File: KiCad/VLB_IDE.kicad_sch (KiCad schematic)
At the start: 9 parts, among them J16 Secondary IDE, U15 OPTI_82C611A

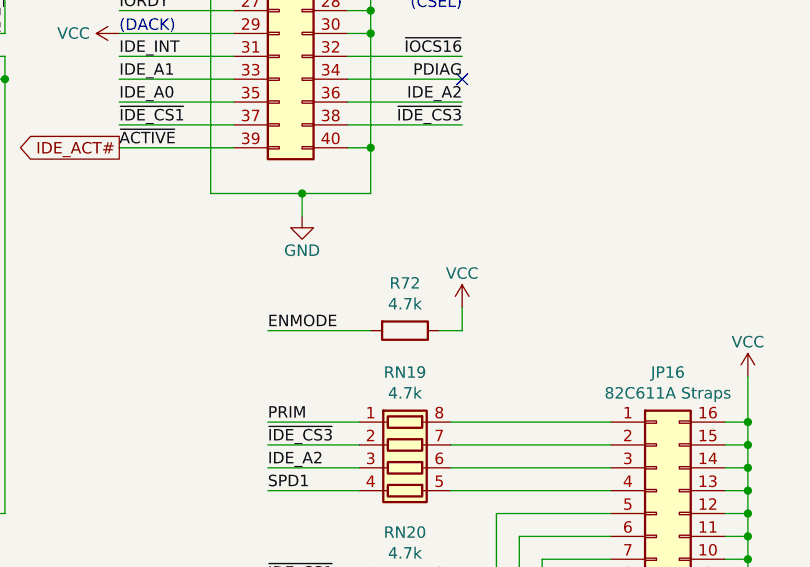
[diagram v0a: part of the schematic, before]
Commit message: Version 0.3: Update DRAM schematic, pull-ups/pull-downs, CPU configuration jumpers
Signed-off-by: Sergey Kiselev <skiselev@gmail.com>
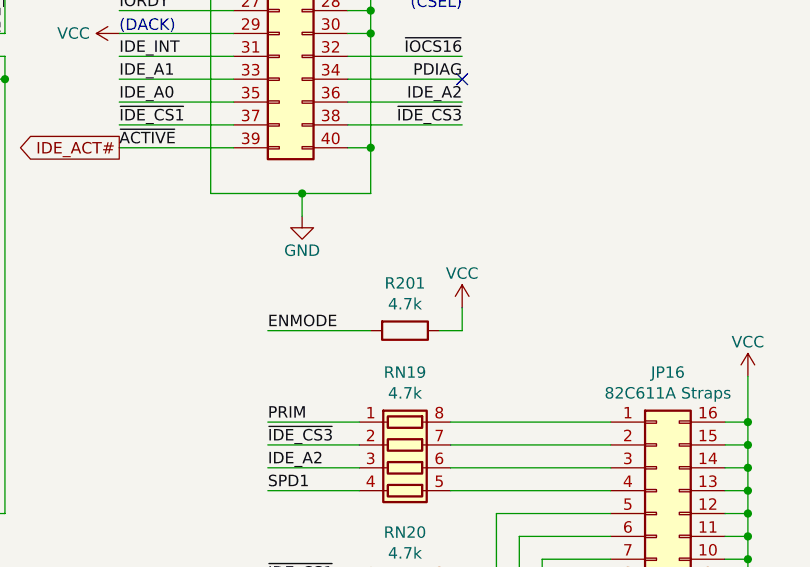
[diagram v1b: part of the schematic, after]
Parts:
- renumbered R72 to R201
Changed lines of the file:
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@@
   (symbol (lib_id "Device:R") (at 196.85 101.6 270) (unit 1)
     (in_bom yes) (on_board yes)
-    (property "Reference" "R72" (id 0) (at 196.85 96.3422 90))
+    (property "Reference" "R201" (id 0) (at 196.85 96.3422 90))
     (property "Value" "4.7k" (id 1) (at 196.85 98.6536 90))
     (property "Footprint" "" (id 2) (at 196.85 99.822 90)

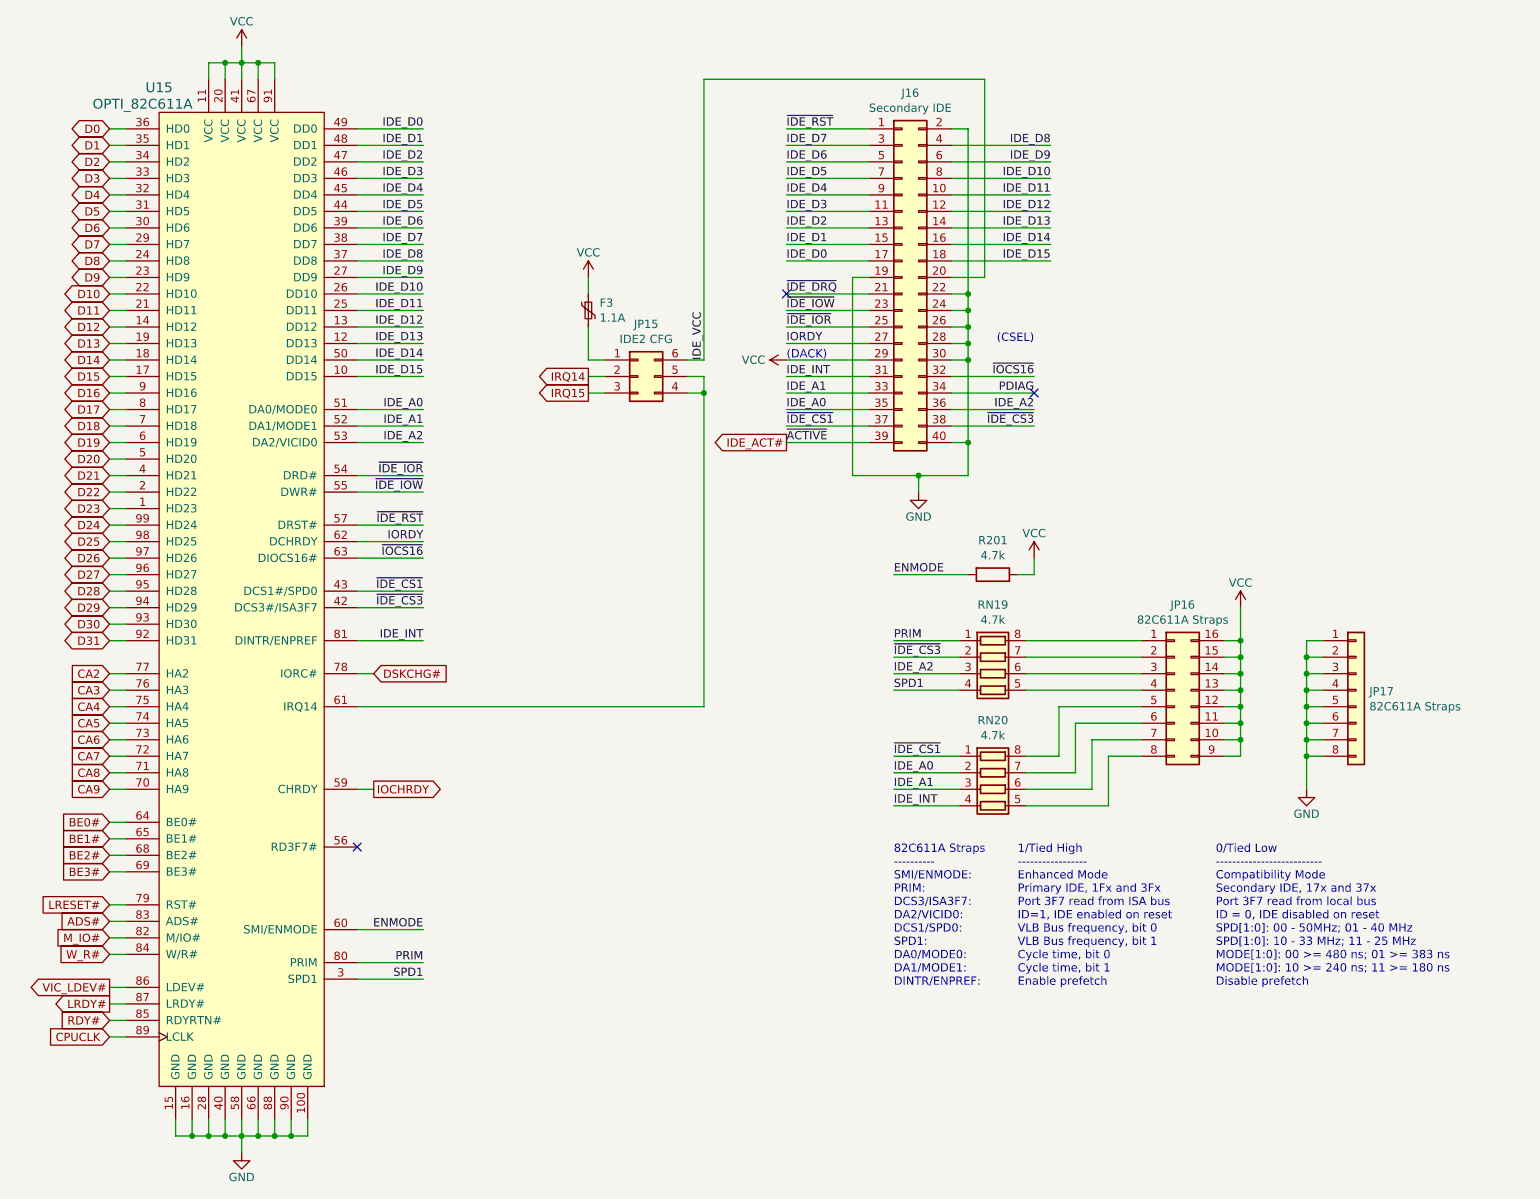
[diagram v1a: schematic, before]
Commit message: Version 0.4: Update chipset connection
Signed-off-by: Sergey Kiselev <skiselev@gmail.com>
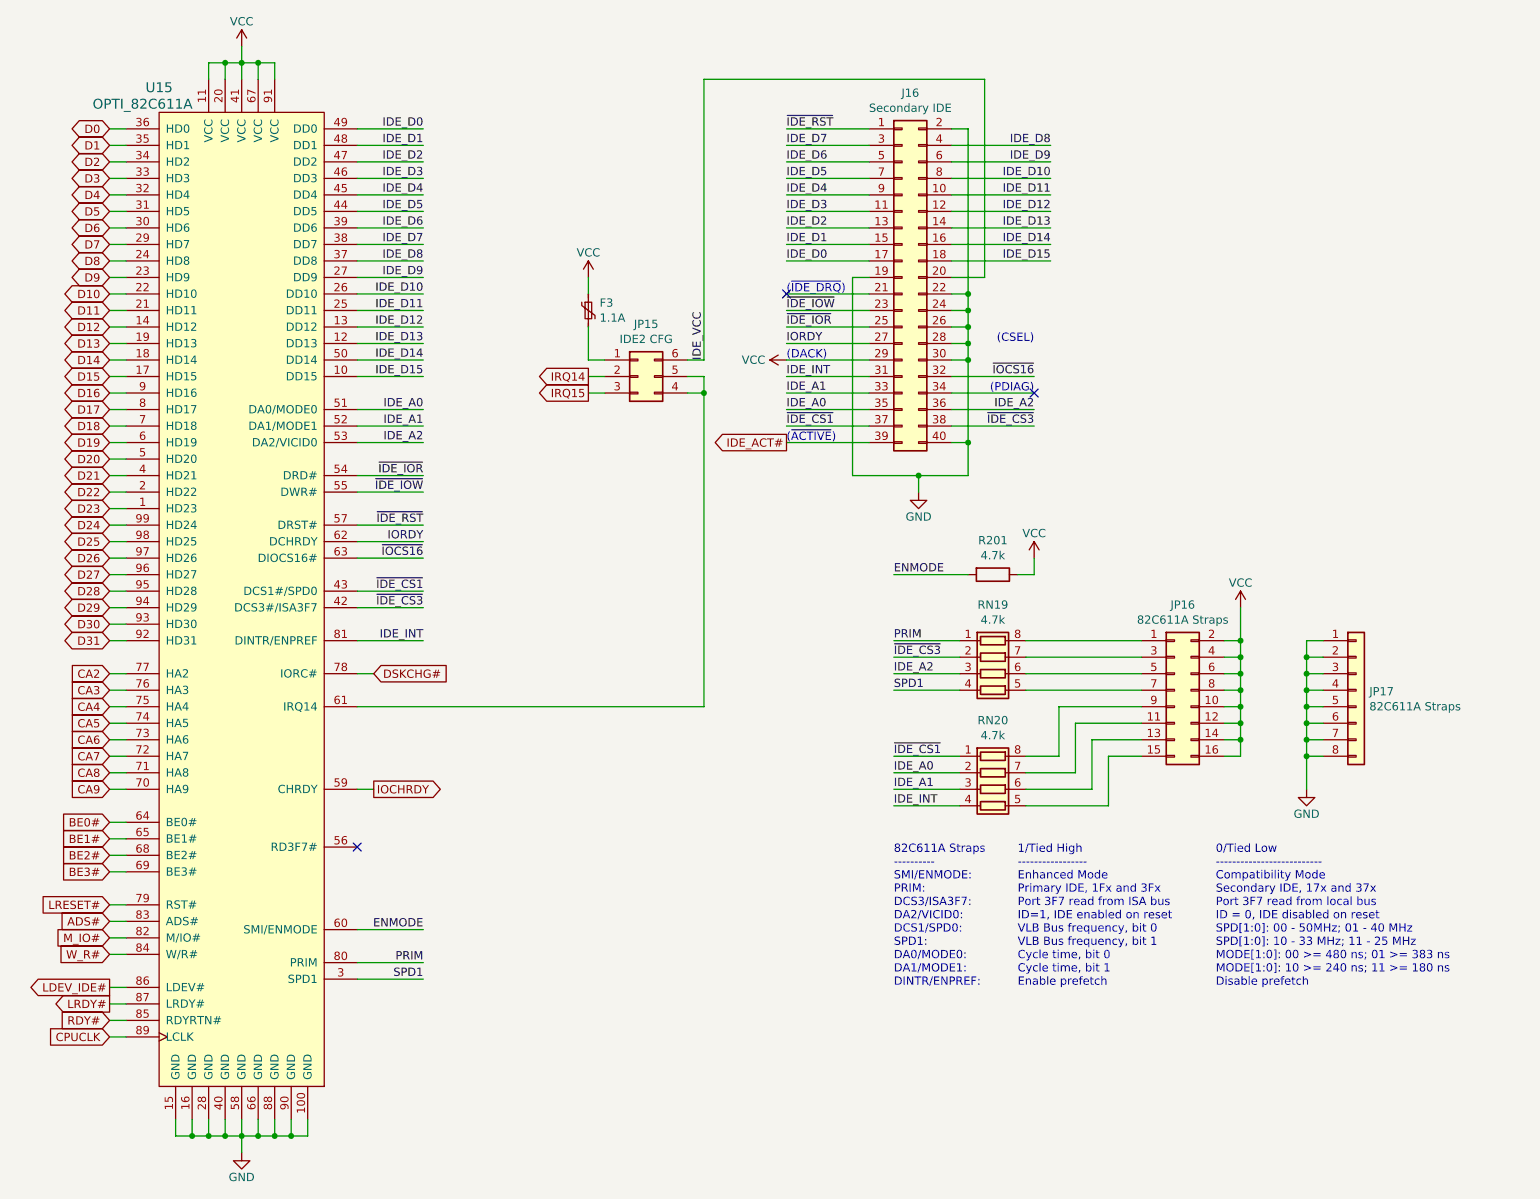
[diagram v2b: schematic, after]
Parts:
- F3: footprint (none) -> Fuse:Fuse_Littelfuse_395Series
- J16: footprint (none) -> My_Components:Conn_Pin_Header_20x2_2.54mm
- JP15: footprint (none) -> My_Components:Conn_Pin_Header_2x3_2.54mm
- JP16: footprint (none) -> My_Components:Conn_Pin_Header_8x2_2.54mm; symbol Connector_Generic:Conn_02x08_Counter_Clockwise -> Connector_Generic:Conn_02x08_Odd_Even
- JP17: footprint (none) -> My_Components:Conn_Pin_Header_8x1_2.54mm
- R201: footprint (none) -> Resistor_SMD:R_0612_1632Metric_Pad1.18x3.40mm_HandSolder
- RN19, RN20: footprint (none) -> Resistor_THT:R_Array_SIP8
- U15: footprint (none) -> My_Components:IC_PQFP-100_14x20mm_P0.65mm_Hand_Soldering
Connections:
- net VCC: now also JP16.2 (Pin_2), JP16.4 (Pin_4), JP16.6 (Pin_6), JP16.8 (Pin_8); no longer JP16.11 (Pin_11), JP16.13 (Pin_13), JP16.15 (Pin_15), JP16.9 (Pin_9)
- net at RN19.5 (R4.2): now also JP16.7 (Pin_7); no longer JP16.4 (Pin_4)
- net at RN19.6 (R3.2): now also JP16.5 (Pin_5); no longer JP16.3 (Pin_3)
- net at RN19.7 (R2.2): now also JP16.3 (Pin_3); no longer JP16.2 (Pin_2)
- net at RN20.5 (R4.2): now also JP16.15 (Pin_15); no longer JP16.8 (Pin_8)
- net at RN20.6 (R3.2): now also JP16.13 (Pin_13); no longer JP16.7 (Pin_7)
- net at RN20.7 (R2.2): now also JP16.11 (Pin_11); no longer JP16.6 (Pin_6)
- net at RN20.8 (R1.2): now also JP16.9 (Pin_9); no longer JP16.5 (Pin_5)
- net PDIAG: no longer names the net of J16.34 (Pin_34)
- net VIC_LDEV# renamed LDEV_IDE#
- net ~{IDE_DRQ}: no longer names the net of J16.21 (Pin_21)
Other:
- note added: "(PDIAG)"
- note added: "(~{ACTIVE})"
- note added: "(~{IDE_DRQ})"
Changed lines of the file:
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@@
     (stroke (width 0) (type default) (color 0 0 0 0))
+  )
+  (text "(~{ACTIVE})" (at 165.1 81.28 0)
+    (effects (font (size 1.27 1.27)) (justify left bottom))
+  )
+  (text "(~{IDE_DRQ})" (at 165.1 58.42 0)
+    (effects (font (size 1.27 1.27)) (justify left bottom))
   )
   (text "1/Tied High\n-----------------\nEnhanced Mode\nPrimary IDE, 1Fx and 3Fx\nPort 3F7 read from ISA bus\nID=1, IDE enabled on reset\nVLB Bus frequency, bit 0\nVLB Bus frequency, bit 1\nCycle time, bit 0\nCycle time, bit 1\nEnable prefetch"
@@
     (effects (font (size 1.27 1.27)) (justify left bottom))
   )
+  (text "(PDIAG)" (at 203.2 73.66 180)
+    (effects (font (size 1.27 1.27)) (justify right bottom))
+  )
   (text "(CSEL)" (at 203.2 66.04 180)
     (effects (font (size 1.27 1.27)) (justify right bottom))
@@
     (effects (font (size 1.27 1.27)) (justify left bottom))
   )
-  (label "~{IDE_DRQ}" (at 165.1 58.42 0)
-    (effects (font (size 1.27 1.27)) (justify left bottom))
-  )
   (label "IDE_D4" (at 165.1 43.18 0)
     (effects (font (size 1.27 1.27)) (justify left bottom))
@@
     (effects (font (size 1.27 1.27)) (justify left bottom))
   )
-  (label "~{ACTIVE}" (at 165.1 81.28 0)
-    (effects (font (size 1.27 1.27)) (justify left bottom))
-  )
   (label "IDE_A0" (at 165.1 76.2 0)
     (effects (font (size 1.27 1.27)) (justify left bottom))
@@
     (effects (font (size 1.27 1.27)) (justify right bottom))
   )
-  (label "PDIAG" (at 203.2 73.66 180)
-    (effects (font (size 1.27 1.27)) (justify right bottom))
-  )
   (label "~{IDE_CS1}" (at 165.1 78.74 0)
     (effects (font (size 1.27 1.27)) (justify left bottom))
@@
     )
   )
-  (global_label "VIC_LDEV#" (shape output) (at 60.96 165.1 180) (fields_autoplaced)
-    (effects (font (size 1.27 1.27)) (justify right))
-    (property "Intersheet References" "${INTERSHEET_REFS}" (id 0) (at 0 0 0)
-      (effects (font (size 1.27 1.27)) hide)
+  (global_label "LDEV_IDE#" (shape output) (at 60.96 165.1 180) (fields_autoplaced)
+    (effects (font (size 1.27 1.27)) (justify right))
+    (property "Intersheet References" "${INTERSHEET_REFS}" (id 0) (at 48.8387 165.0206 0)
+      (effects (font (size 1.27 1.27)) (justify right) hide)
     )
   )
@@
       (effects (font (size 1.524 1.524)))
     )
-    (property "Footprint" "" (id 2) (at 81.28 68.58 0)
-      (effects (font (size 1.524 1.524)))
+    (property "Footprint" "My_Components:IC_PQFP-100_14x20mm_P0.65mm_Hand_Soldering" (id 2) (at 81.28 68.58 0)
+      (effects (font (size 1.524 1.524)) hide)
     )
     (property "Datasheet" "" (id 3) (at 81.28 68.58 0)
@@
     (property "Reference" "J16" (id 0) (at 184.15 27.5082 0))
     (property "Value" "Secondary IDE" (id 1) (at 184.15 29.8196 0))
-    (property "Footprint" "" (id 2) (at 182.88 55.88 0)
+    (property "Footprint" "My_Components:Conn_Pin_Header_20x2_2.54mm" (id 2) (at 182.88 55.88 0)
       (effects (font (size 1.27 1.27)) hide)
     )
@@
       (effects (font (size 1.27 1.27)) (justify left))
     )
-    (property "Footprint" "" (id 2) (at 135.89 66.04 0)
+    (property "Footprint" "Fuse:Fuse_Littelfuse_395Series" (id 2) (at 135.89 66.04 0)
       (effects (font (size 1.27 1.27)) (justify left) hide)
     )
@@
     (property "Reference" "JP15" (id 0) (at 143.51 63.0682 0))
     (property "Value" "IDE2 CFG" (id 1) (at 143.51 65.3796 0))
-    (property "Footprint" "" (id 2) (at 142.24 71.12 0)
+    (property "Footprint" "My_Components:Conn_Pin_Header_2x3_2.54mm" (id 2) (at 142.24 71.12 0)
       (effects (font (size 1.27 1.27)) hide)
     )
@@
     (property "Reference" "RN19" (id 0) (at 196.85 106.2482 90))
     (property "Value" "4.7k" (id 1) (at 196.85 108.5596 90))
-    (property "Footprint" "" (id 2) (at 196.85 123.825 90)
+    (property "Footprint" "Resistor_THT:R_Array_SIP8" (id 2) (at 196.85 123.825 90)
       (effects (font (size 1.27 1.27)) hide)
     )
@@
     (property "Reference" "RN20" (id 0) (at 196.85 124.0282 90))
     (property "Value" "4.7k" (id 1) (at 196.85 126.3396 90))
-    (property "Footprint" "" (id 2) (at 196.85 141.605 90)
+    (property "Footprint" "Resistor_THT:R_Array_SIP8" (id 2) (at 196.85 141.605 90)
       (effects (font (size 1.27 1.27)) hide)
     )
@@
     (pin "8")
   )
-  (symbol (lib_id "Connector_Generic:Conn_02x08_Counter_Clockwise") (at 224.79 119.38 0) (unit 1)
+  (symbol (lib_id "Connector_Generic:Conn_02x08_Odd_Even") (at 224.79 119.38 0) (unit 1)
     (in_bom yes) (on_board yes)
     (property "Reference" "JP16" (id 0) (at 226.06 106.2482 0))
     (property "Value" "82C611A Straps" (id 1) (at 226.06 108.5596 0))
-    (property "Footprint" "" (id 2) (at 224.79 119.38 0)
+    (property "Footprint" "My_Components:Conn_Pin_Header_8x2_2.54mm" (id 2) (at 224.79 119.38 0)
       (effects (font (size 1.27 1.27)) hide)
     )
@@
       (effects (font (size 1.27 1.27)) (justify left))
     )
-    (property "Footprint" "" (id 2) (at 252.73 119.38 0)
+    (property "Footprint" "My_Components:Conn_Pin_Header_8x1_2.54mm" (id 2) (at 252.73 119.38 0)
       (effects (font (size 1.27 1.27)) hide)
     )
@@
     (property "Reference" "R201" (id 0) (at 196.85 96.3422 90))
     (property "Value" "4.7k" (id 1) (at 196.85 98.6536 90))
-    (property "Footprint" "" (id 2) (at 196.85 99.822 90)
-      (effects (font (size 1.27 1.27)) hide)
-    )
+    (property "Footprint" "Resistor_SMD:R_0612_1632Metric_Pad1.18x3.40mm_HandSolder" (id 2) (at 196.85 99.822 90)
+      (effects (font (size 1.27 1.27)) hide)
+    )
